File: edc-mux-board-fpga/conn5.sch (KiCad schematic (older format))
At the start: 24 parts

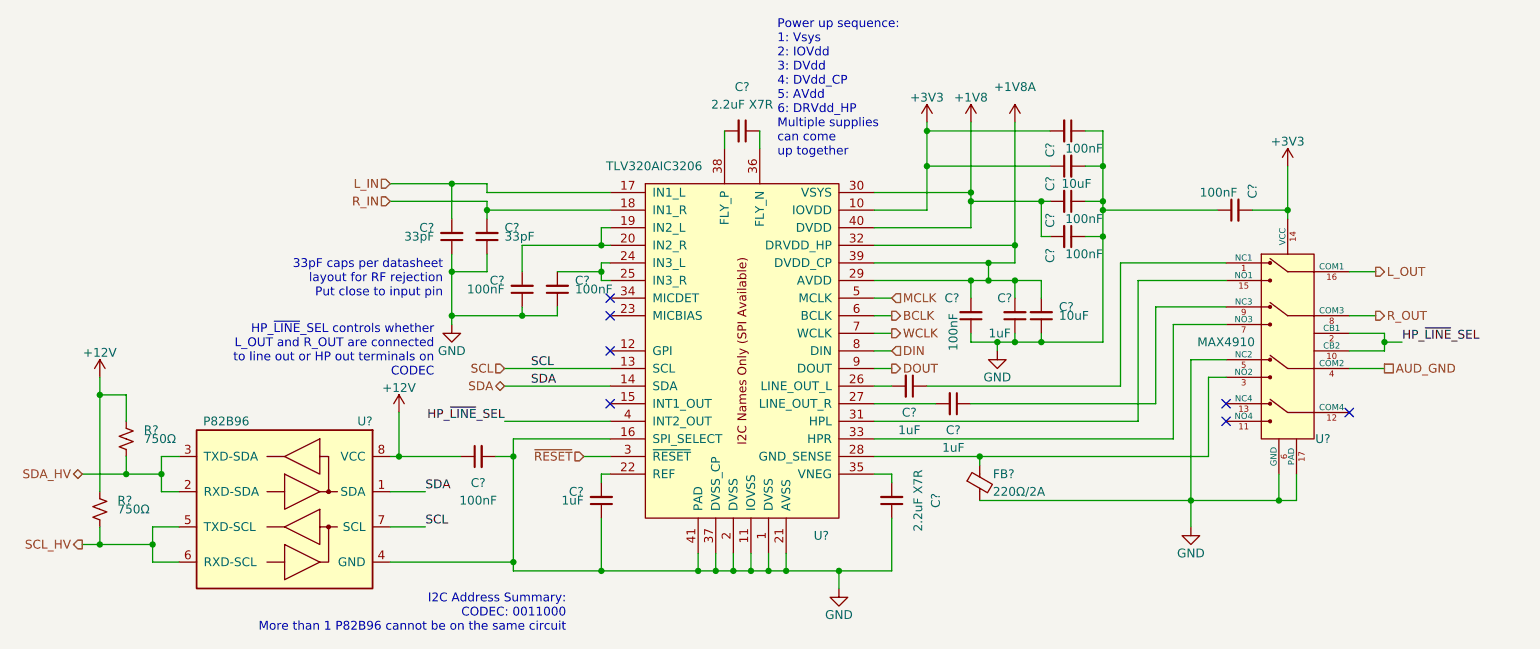
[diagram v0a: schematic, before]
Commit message: Finished FPGA and MCU interconnections.
Finished up interrupt wiring
Fixed a few missing connections
Annotated Schematic
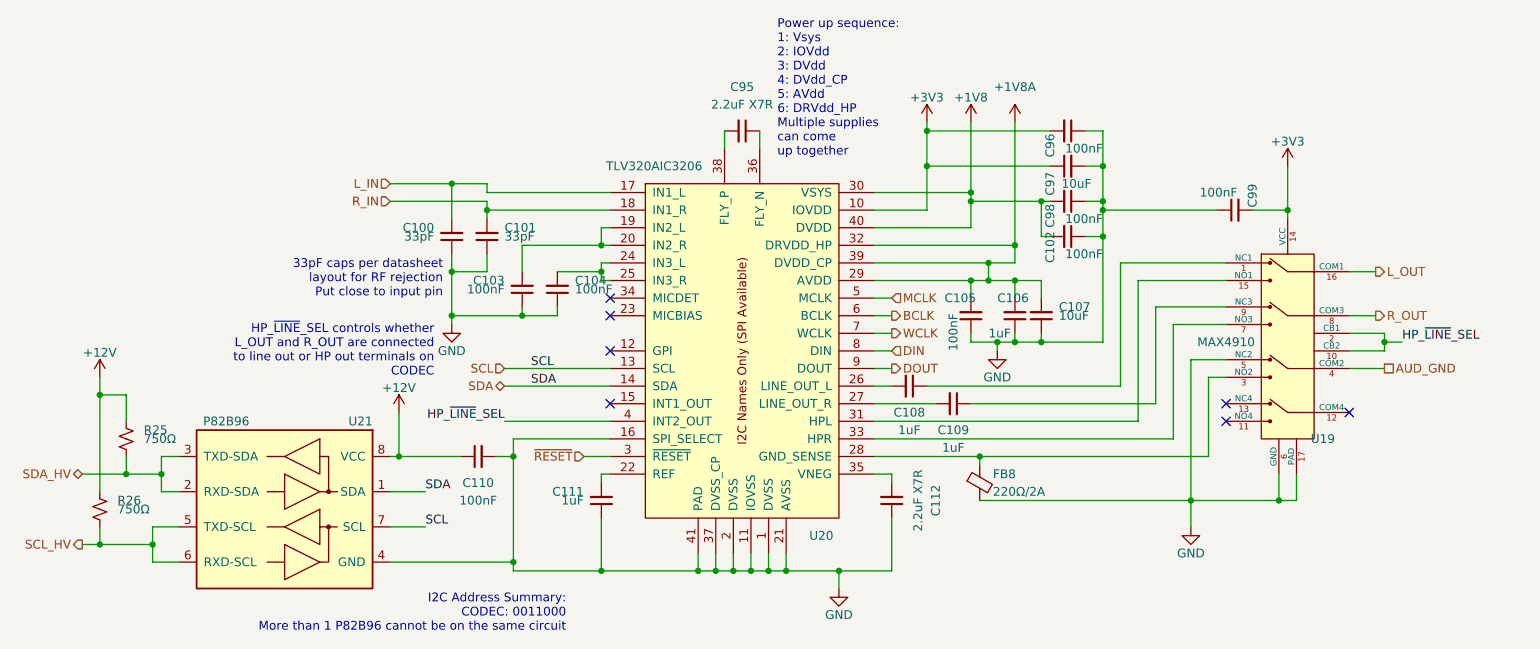
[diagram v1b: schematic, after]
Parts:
- removed C? (x2): 1uF, Capacitor_SMD:C_0805_2012Metric, symbol Device:C_Small
- removed C? (x2): 2.2uF X7R, Capacitor_SMD:C_0603_1608Metric, symbol Device:C_Small
- removed C?: 1uF, Capacitor_SMD:C_0603_1608Metric, symbol Device:C_Small
- removed C? (x8): 100nF, Capacitor_SMD:C_0603_1608Metric, symbol Device:C_Small
- removed C? (x2): 33pF, Capacitor_SMD:C_0603_1608Metric, symbol Device:C_Small
- removed C? (x2): 10uF, Capacitor_SMD:C_1206_3216Metric, symbol Device:C_Small
- removed FB?: 220Ω/2A, Resistor_SMD:R_0603_1608Metric, symbol Device:Ferrite_Bead_Small
- removed R? (x2): 750Ω, Resistor_SMD:R_0603_1608Metric, symbol Device:R_Small_US
- removed U?: TLV320AIC3206, Package_DFN_QFN:UQFN-40-1EP_5x5mm_P0.4mm_EP3.8x3.8mm_ThermalVias, symbol SW-Texas:TLV320AIC3206
- removed U?: MAX4910, Package_DFN_QFN:TQFN-16-1EP_3x3mm_P0.5mm_EP1.23x1.23mm, symbol SW-dallas-semi-maxim:MAX4910
- removed U?: P82B96, Package_SO:TSSOP-8_3x3mm_P0.65mm, symbol Interface_Expansion:P82B96
- added C100, C101: 33pF, Capacitor_SMD:C_0603_1608Metric, symbol Device:C_Small
- added C102, C103, C104, C105, C110, C96, C98, C99: 100nF, Capacitor_SMD:C_0603_1608Metric, symbol Device:C_Small
- added C107, C97: 10uF, Capacitor_SMD:C_1206_3216Metric, symbol Device:C_Small
- added C108, C109: 1uF, Capacitor_SMD:C_0805_2012Metric, symbol Device:C_Small
- added C111: 1uF, Capacitor_SMD:C_0603_1608Metric, symbol Device:C_Small
- added C112, C95: 2.2uF X7R, Capacitor_SMD:C_0603_1608Metric, symbol Device:C_Small
- added FB8: 220Ω/2A, Resistor_SMD:R_0603_1608Metric, symbol Device:Ferrite_Bead_Small
- added R25, R26: 750Ω, Resistor_SMD:R_0603_1608Metric, symbol Device:R_Small_US
- added U19: MAX4910, Package_DFN_QFN:TQFN-16-1EP_3x3mm_P0.5mm_EP1.23x1.23mm, symbol SW-dallas-semi-maxim:MAX4910
- added U20: TLV320AIC3206, Package_DFN_QFN:UQFN-40-1EP_5x5mm_P0.4mm_EP3.8x3.8mm_ThermalVias, symbol SW-Texas:TLV320AIC3206
- added U21: P82B96, Package_SO:TSSOP-8_3x3mm_P0.65mm, symbol Interface_Expansion:P82B96
- gave numbers to parts that had none: 1
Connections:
- net +12V: now also C110.1, R25.1, R26.1, U21.8 (VCC)
- net +1V8: now also C102.2, C98.2, U20.30 (VSYS), U20.40 (DVDD)
- net +1V8A: now also C105.2, C107.2, U20.29 (AVDD), U20.32 (DRVDD_HP), U20.39 (DVDD_CP)
- net +3V3: now also C96.2, C97.1, C99.2, U19.14 (VCC), U20.10 (IOVDD)
- net AUD_GND: now also U19.4 (COM2)
- net BCLK: now also U20.6 (BCLK)
- net DIN: now also U20.8 (DIN)
- net DOUT: now also U20.9 (DOUT)
- net GND: now also C100.1, C101.1, C102.1, C103.1, C104.1, C105.1, C107.1, C110.2, C111.1, C112.1, C96.1, C97.2, C98.1, C99.1, FB8.2, U19.17 (PAD), U19.5 (NC2), U19.6 (GND), U20.1 (DVSS), U20.11 (IOVSS), U20.16 (SPI_SELECT), U20.2 (DVSS), U20.21 (AVSS), U20.37 (DVSS_CP), U20.41 (PAD), U21.4 (GND)
- net HP_~LINE~_SEL: now also U19.10 (CB2), U19.2 (CB1), U20.4 (INT2_OUT)
- net L_IN: now also C100.2, U20.17 (IN1_L)
- net L_OUT: now also U19.16 (COM1)
- net MCLK: now also U20.5 (MCLK)
- net R_IN: now also C101.2, U20.18 (IN1_R)
- net R_OUT: now also U19.8 (COM3)
- net SCL: now also U20.13 (SCL), U21.7 (SCL)
- net SCL_HV: now also R26.2, U21.5 (TXD-SCL), U21.6 (RXD-SCL)
- net SDA: now also U20.14 (SDA), U21.1 (SDA)
- net SDA_HV: now also R25.2, U21.2 (RXD-SDA), U21.3 (TXD-SDA)
- net WCLK: now also U20.7 (WCLK)
- net ~RESET: now also U20.3 (~RESET)
- new net: C108.1, U19.1 (NC1)
- new net: C108.2, U20.26 (LINE_OUT_L)
- new net: C109.1, U19.9 (NC3)
- new net: C109.2, U20.27 (LINE_OUT_R)
- new net: C103.2, U20.19 (IN2_L), U20.20 (IN2_R)
- new net: C111.2, U20.22 (REF)
- new net: C104.2, U20.24 (IN3_L), U20.25 (IN3_R)
- new net: FB8.1, U19.3 (NO2), U20.28 (GND_SENSE)
- new net: U19.15 (NO1), U20.31 (HPL)
- new net: U19.7 (NO3), U20.33 (HPR)
- new net: C112.2, U20.35 (VNEG)
- new net: C95.1, U20.36 (FLY_N)
- new net: C95.2, U20.38 (FLY_P)
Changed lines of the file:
@@
 $EndDescr
 $Comp
-L SW-Texas:TLV320AIC3206 U?
-U 1 1 5CE6F2E7
+L SW-Texas:TLV320AIC3206 U20
+U 1 1 5DAC04B0
 P 5200 3400
-F 0 "U?" H 5650 2350 50  0000 C CNN
+F 0 "U20" H 5650 2350 50  0000 C CNN
 F 1 "TLV320AIC3206" H 4700 4450 50  0000 C CNN
 F 2 "Package_DFN_QFN:UQFN-40-1EP_5x5mm_P0.4mm_EP3.8x3.8mm_ThermalVias" H 5250 4800 50  0001 C CNN
@@
 $EndComp
 $Comp
-L Device:C_Small C?
-U 1 1 5CE6F309
+L Device:C_Small C95
+U 1 1 5DAC04C8
 P 5200 2150
-F 0 "C?" V 4950 2150 50  0000 C CNN
+F 0 "C95" V 4950 2150 50  0000 C CNN
 F 1 "2.2uF X7R" V 5050 2150 50  0000 C CNN
 F 2 "Capacitor_SMD:C_0603_1608Metric" H 5200 2150 50  0001 C CNN
@@
 	5300 2250 5300 2150
 $Comp
-L Device:C_Small C?
-U 1 1 5CE6F311
+L Device:C_Small C112
+U 1 1 5DAC04CE
 P 6050 4250
-F 0 "C?" V 5800 4250 50  0000 C CNN
+F 0 "C112" V 5800 4250 50  0000 C CNN
 F 1 "2.2uF X7R" V 5900 4250 50  0000 C CNN
 F 2 "Capacitor_SMD:C_0603_1608Metric" H 6050 4250 50  0001 C CNN
@@
 	6050 4100 6050 4150
 $Comp
-L power:GND #PWR?
-U 1 1 5CE6F323
+L power:GND #PWR073
+U 1 1 5DAC04E8
 P 5750 4750
-F 0 "#PWR?" H 5750 4500 50  0001 C CNN
+F 0 "#PWR073" H 5750 4500 50  0001 C CNN
 F 1 "GND" H 5750 4600 50  0000 C CNN
 F 2 "" H 5750 4750 50  0001 C CNN
@@
 	5450 4650 5750 4650
 $Comp
-L Device:C_Small C?
-U 1 1 5CE6F329
+L Device:C_Small C111
+U 1 1 5DAC04ED
 P 4400 4250
-F 0 "C?" H 4500 4200 50  0000 L CNN
+F 0 "C111" H 4500 4200 50  0000 L CNN
 F 1 "1uF" H 4500 4250 50  0000 L CNN
 F 2 "Capacitor_SMD:C_0603_1608Metric" H 4400 4250 50  0001 C CNN
@@
 Connection ~ 4950 4650
 $Comp
-L Device:C_Small C?
-U 1 1 5CE6F348
+L Device:C_Small C103
+U 1 1 5DAC04FB
 P 3950 3050
-F 0 "C?" H 4050 3000 50  0000 L CNN
+F 0 "C103" H 4050 3000 50  0000 L CNN
 F 1 "100nF" H 4050 3050 50  0000 L CNN
 F 2 "Capacitor_SMD:C_0603_1608Metric" H 3950 3050 50  0001 C CNN
@@
 $EndComp
 $Comp
-L Device:C_Small C?
-U 1 1 5CE6F363
+L Device:C_Small C104
+U 1 1 5DAC0515
 P 4150 3050
-F 0 "C?" H 4050 3000 50  0000 R CNN
+F 0 "C104" H 4050 3000 50  0000 R CNN
 F 1 "100nF" H 4050 3050 50  0000 R CNN
 F 2 "Capacitor_SMD:C_0603_1608Metric" H 4150 3050 50  0001 C CNN
@@
 Connection ~ 4400 2950
 $Comp
-L power:GND #PWR?
-U 1 1 5CE6F368
+L power:GND #PWR068
+U 1 1 5DAC051A
 P 3550 3250
-F 0 "#PWR?" H 3550 3000 50  0001 C CNN
+F 0 "#PWR068" H 3550 3000 50  0001 C CNN
 F 1 "GND" H 3550 3100 50  0000 C CNN
 F 2 "" H 3550 3250 50  0001 C CNN
@@
 	8650 3300 8850 3300
 $Comp
-L SW-dallas-semi-maxim:MAX4910 U?
-U 1 1 5CE6F375
+L SW-dallas-semi-maxim:MAX4910 U19
+U 1 1 5DAC0532
 P 8300 3350
-F 0 "U?" H 8500 2800 50  0000 C CNN
+F 0 "U19" H 8500 2800 50  0000 C CNN
 F 1 "MAX4910" H 7950 3350 50  0000 C CNN
 F 2 "Package_DFN_QFN:TQFN-16-1EP_3x3mm_P0.5mm_EP1.23x1.23mm" H 9950 4500 50  0001 C CNN
@@
 	7750 3450 7750 4250
 $Comp
-L power:GND #PWR?
-U 1 1 5CE6F387
+L power:GND #PWR072
+U 1 1 5DAC0537
 P 7750 4400
-F 0 "#PWR?" H 7750 4150 50  0001 C CNN
+F 0 "#PWR072" H 7750 4150 50  0001 C CNN
 F 1 "GND" H 7750 4250 50  0000 C CNN
 F 2 "" H 7750 4400 50  0001 C CNN
@@
 	8650 3500 8850 3500
 $Comp
-L Device:Ferrite_Bead_Small FB?
-U 1 1 5CE6F39A
+L Device:Ferrite_Bead_Small FB8
+U 1 1 5DAC054C
 P 6550 4150
-F 0 "FB?" H 6625 4200 50  0000 L CNN
+F 0 "FB8" H 6625 4200 50  0000 L CNN
 F 1 "220Ω/2A" H 6625 4100 50  0000 L CNN
 F 2 "Resistor_SMD:R_0603_1608Metric" V 6480 4150 50  0001 C CNN
@@
 	3750 2600 4450 2600
 $Comp
-L Device:C_Small C?
-U 1 1 5CE6F3AC
+L Device:C_Small C100
+U 1 1 5DAC0553
 P 3550 2750
-F 0 "C?" H 3650 2700 50  0000 L CNN
+F 0 "C100" H 3650 2700 50  0000 L CNN
 F 1 "33pF" H 3650 2750 50  0000 L CNN
 F 2 "Capacitor_SMD:C_0603_1608Metric" H 3550 2750 50  0001 C CNN
@@
 	3200 2550 3750 2550
 $Comp
-L Device:C_Small C?
-U 1 1 5CE6F3B7
+L Device:C_Small C101
+U 1 1 5DAC056F
 P 3750 2750
-F 0 "C?" H 3650 2700 50  0000 R CNN
+F 0 "C101" H 3650 2700 50  0000 R CNN
 F 1 "33pF" H 3650 2750 50  0000 R CNN
 F 2 "Capacitor_SMD:C_0603_1608Metric" H 3750 2750 50  0001 C CNN
@@
 	5950 3000 6500 3000
 $Comp
-L SW-power:+1V8A #+1V8A?
-U 1 1 5CE6F3C8
+L SW-power:+1V8A #+1V8A07
+U 1 1 5DAC0574
 P 6750 2100
-F 0 "#+1V8A?" H 7500 1800 60  0001 C CNN
+F 0 "#+1V8A07" H 7500 1800 60  0001 C CNN
 F 1 "+1V8A" H 6750 2300 50  0000 C CNN
 F 2 "" H 6750 2100 60  0001 C CNN
@@
 $EndComp
 $Comp
-L power:+1V8 #PWR?
-U 1 1 5CE6F3D1
+L power:+1V8 #PWR066
+U 1 1 5DAC0583
 P 6500 2100
-F 0 "#PWR?" H 6500 1950 50  0001 C CNN
+F 0 "#PWR066" H 6500 1950 50  0001 C CNN
 F 1 "+1V8" H 6500 2240 50  0000 C CNN
 F 2 "" H 6500 2100 50  0001 C CNN
@@
 	6750 2800 6750 2900
 $Comp
-L power:+3V3 #PWR?
-U 1 1 5CE6F3E5
+L power:+3V3 #PWR065
+U 1 1 5DAC0598
 P 6250 2100
-F 0 "#PWR?" H 6250 1950 50  0001 C CNN
+F 0 "#PWR065" H 6250 1950 50  0001 C CNN
 F 1 "+3V3" H 6250 2240 50  0000 C CNN
 F 2 "" H 6250 2100 50  0001 C CNN
@@
 	6250 2600 6250 2350
 $Comp
-L Device:C_Small C?
+L Device:C_Small C106
 U 1 1 5CE6F3F4
 P 6750 3200
-F 0 "C?" H 6850 3100 50  0000 R CNN
+F 0 "C106" H 6850 3100 50  0000 R CNN
 F 1 "1uF" H 6900 3300 50  0000 R CNN
 F 2 "Capacitor_SMD:C_0603_1608Metric" H 6750 3200 50  0001 C CNN
@@
 $EndComp
 $Comp
-L power:GND #PWR?
-U 1 1 5CE6F403
+L power:GND #PWR069
+U 1 1 5DAC05AE
 P 6650 3400
-F 0 "#PWR?" H 6650 3150 50  0001 C CNN
+F 0 "#PWR069" H 6650 3150 50  0001 C CNN
 F 1 "GND" H 6650 3250 50  0000 C CNN
 F 2 "" H 6650 3400 50  0001 C CNN
@@
 $EndComp
 $Comp
-L Device:C_Small C?
-U 1 1 5CE6F40F
+L Device:C_Small C107
+U 1 1 5DAC05C8
 P 6900 3200
-F 0 "C?" H 6800 3150 50  0000 R CNN
+F 0 "C107" H 6800 3150 50  0000 R CNN
 F 1 "10uF" H 6800 3200 50  0000 R CNN
 F 2 "Capacitor_SMD:C_1206_3216Metric" H 6900 3200 50  0001 C CNN
@@
 $EndComp
 $Comp
-L Device:C_Small C?
-U 1 1 5CE6F425
+L Device:C_Small C105
+U 1 1 5DAC05CA
 P 6500 3200
-F 0 "C?" H 6650 3100 50  0000 R CNN
+F 0 "C105" H 6650 3100 50  0000 R CNN
 F 1 "100nF" V 6600 3400 50  0000 R CNN
 F 2 "Capacitor_SMD:C_0603_1608Metric" H 6500 3200 50  0001 C CNN
@@
 	6650 3350 6750 3350
 $Comp
-L Device:C_Small C?
-U 1 1 5CE6F42F
+L Device:C_Small C96
+U 1 1 5DAC05DB
 P 7050 2150
-F 0 "C?" H 7200 2050 50  0000 R CNN
+F 0 "C96" H 7200 2050 50  0000 R CNN
 F 1 "100nF" V 7150 2350 50  0000 R CNN
 F 2 "Capacitor_SMD:C_0603_1608Metric" H 7050 2150 50  0001 C CNN
@@
 $EndComp
 $Comp
-L Device:C_Small C?
-U 1 1 5CE6F439
+L Device:C_Small C97
+U 1 1 5DAC05F1
 P 7050 2350
-F 0 "C?" H 6950 2450 50  0000 C CNN
+F 0 "C97" H 6950 2450 50  0000 C CNN
 F 1 "10uF" V 6950 2300 50  0000 C CNN
 F 2 "Capacitor_SMD:C_1206_3216Metric" H 7050 2350 50  0001 C CNN
@@
 	6250 2150 6250 2100
 $Comp
-L Device:C_Small C?
-U 1 1 5CE6F451
+L Device:C_Small C98
+U 1 1 5DAC05FF
 P 7050 2550
-F 0 "C?" H 7200 2450 50  0000 R CNN
+F 0 "C98" H 7200 2450 50  0000 R CNN
 F 1 "100nF" V 7150 2750 50  0000 R CNN
 F 2 "Capacitor_SMD:C_0603_1608Metric" H 7050 2550 50  0001 C CNN
@@
 	6500 2550 6500 2500
 $Comp
-L Device:C_Small C?
-U 1 1 5CE6F456
+L Device:C_Small C102
+U 1 1 5DAC060C
 P 7050 2750
-F 0 "C?" H 7200 2650 50  0000 R CNN
+F 0 "C102" H 7200 2650 50  0000 R CNN
 F 1 "100nF" V 7150 2950 50  0000 R CNN
 F 2 "Capacitor_SMD:C_0603_1608Metric" H 7050 2750 50  0001 C CNN
@@
 NoConn ~ 8650 3750
 $Comp
-L Device:C_Small C?
-U 1 1 5CE6F46F
+L Device:C_Small C99
+U 1 1 5DAC061E
 P 8000 2600
-F 0 "C?" H 8150 2500 50  0000 R CNN
+F 0 "C99" H 8150 2500 50  0000 R CNN
 F 1 "100nF" V 8100 2800 50  0000 R CNN
 F 2 "Capacitor_SMD:C_0603_1608Metric" H 8000 2600 50  0001 C CNN
@@
 $EndComp
 $Comp
-L power:+3V3 #PWR?
-U 1 1 5CE6F47E
+L power:+3V3 #PWR067
+U 1 1 5DAC062E
 P 8300 2350
-F 0 "#PWR?" H 8300 2200 50  0001 C CNN
+F 0 "#PWR067" H 8300 2200 50  0001 C CNN
 F 1 "+3V3" H 8300 2490 50  0000 C CNN
 F 2 "" H 8300 2350 50  0001 C CNN
@@
 	8250 4250 8350 4250
 $Comp
-L Interface_Expansion:P82B96 U?
-U 1 1 5CE6F489
+L Interface_Expansion:P82B96 U21
+U 1 1 5DAC0634
 P 2600 4300
-F 0 "U?" H 2100 4800 50  0000 L CNN
+F 0 "U21" H 2100 4800 50  0000 L CNN
 F 1 "P82B96" H 2800 4800 50  0000 L CNN
 F 2 "Package_SO:TSSOP-8_3x3mm_P0.65mm" H 2600 4300 50  0001 C CNN
@@
 $EndComp
 $Comp
-L power:+12V #PWR?
-U 1 1 5CE6F490
+L power:+12V #PWR070
+U 1 1 5DAC064C
 P 1550 3550
-F 0 "#PWR?" H 1550 3400 50  0001 C CNN
+F 0 "#PWR070" H 1550 3400 50  0001 C CNN
 F 1 "+12V" H 1550 3690 50  0000 C CNN
 F 2 "" H 1550 3550 50  0001 C CNN
@@
 	1900 4100 1900 4200
 $Comp
-L Device:R_Small_US R?
-U 1 1 5CE6F4C1
+L Device:R_Small_US R25
+U 1 1 5DAC065F
 P 1700 3900
-F 0 "R?" H 1800 3950 50  0000 L CNN
+F 0 "R25" H 1800 3950 50  0000 L CNN
 F 1 "750Ω" H 1800 3900 50  0000 L CNN
 F 2 "Resistor_SMD:R_0603_1608Metric" H 1700 3900 50  0001 C CNN
@@
 $EndComp
 $Comp
-L Device:R_Small_US R?
-U 1 1 5CE6F4D0
+L Device:R_Small_US R26
+U 1 1 5DAC0660
 P 1550 4300
-F 0 "R?" H 1650 4350 50  0000 L CNN
+F 0 "R26" H 1650 4350 50  0000 L CNN
 F 1 "750Ω" H 1650 4300 50  0000 L CNN
 F 2 "Resistor_SMD:R_0603_1608Metric" H 1550 4300 50  0001 C CNN
@@
 	1700 4100 1900 4100
 $Comp
-L power:+12V #PWR?
+L power:+12V #PWR071
 U 1 1 5CE6F4E1
 P 3250 3750
-F 0 "#PWR?" H 3250 3600 50  0001 C CNN
+F 0 "#PWR071" H 3250 3600 50  0001 C CNN
 F 1 "+12V" H 3250 3890 50  0000 C CNN
 F 2 "" H 3250 3750 50  0001 C CNN
@@
 	3200 4400 3400 4400
 $Comp
-L Device:C_Small C?
-U 1 1 5CE6F4F3
+L Device:C_Small C110
+U 1 1 5DAC067F
 P 3700 4000
-F 0 "C?" V 3550 4000 50  0000 C CNN
+F 0 "C110" V 3550 4000 50  0000 C CNN
 F 1 "100nF" V 3450 4000 50  0000 C CNN
 F 2 "Capacitor_SMD:C_0603_1608Metric" H 3700 4000 50  0001 C CNN
@@
 	1450 4500 1550 4500
 $Comp
-L Device:C_Small C?
-U 1 1 5CE6F2C0
+L Device:C_Small C108
+U 1 1 5DAC049A
 P 6150 3600
-F 0 "C?" V 6300 3600 50  0000 C CNN
+F 0 "C108" V 6300 3600 50  0000 C CNN
 F 1 "1uF" V 6400 3600 50  0000 C CNN
 F 2 "Capacitor_SMD:C_0805_2012Metric" H 6150 3600 50  0001 C CNN
@@
 $EndComp
 $Comp
-L Device:C_Small C?
-U 1 1 5CE6F2D4
+L Device:C_Small C109
+U 1 1 5DAC04A7
 P 6400 3700
-F 0 "C?" V 6550 3700 50  0000 C CNN
+F 0 "C109" V 6550 3700 50  0000 C CNN
 F 1 "1uF" V 6650 3700 50  0000 C CNN
 F 2 "Capacitor_SMD:C_0805_2012Metric" H 6400 3700 50  0001 C CNN

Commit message: assigned more footprints
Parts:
- C106, C111: value 1uF -> 1uF X7R
- C107, C97: value 10uF -> 10uF X7R
- C108, C109: value 1uF -> 1uF X7R flex
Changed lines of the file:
@@
 P 4400 4250
 F 0 "C111" H 4500 4200 50  0000 L CNN
-F 1 "1uF" H 4500 4250 50  0000 L CNN
+F 1 "1uF X7R" H 4500 4250 50  0000 L CNN
 F 2 "Capacitor_SMD:C_0603_1608Metric" H 4400 4250 50  0001 C CNN
 F 3 "~" H 4400 4250 50  0001 C CNN
@@
 P 6750 3200
 F 0 "C106" H 6850 3100 50  0000 R CNN
-F 1 "1uF" H 6900 3300 50  0000 R CNN
+F 1 "1uF X7R" H 6900 3300 50  0000 R CNN
 F 2 "Capacitor_SMD:C_0603_1608Metric" H 6750 3200 50  0001 C CNN
 F 3 "~" H 6750 3200 50  0001 C CNN
@@
 P 6900 3200
 F 0 "C107" H 6800 3150 50  0000 R CNN
-F 1 "10uF" H 6800 3200 50  0000 R CNN
+F 1 "10uF X7R" H 6800 3200 50  0000 R CNN
 F 2 "Capacitor_SMD:C_1206_3216Metric" H 6900 3200 50  0001 C CNN
 F 3 "~" H 6900 3200 50  0001 C CNN
@@
 P 7050 2350
 F 0 "C97" H 6950 2450 50  0000 C CNN
-F 1 "10uF" V 6950 2300 50  0000 C CNN
+F 1 "10uF X7R" V 6950 2300 50  0000 C CNN
 F 2 "Capacitor_SMD:C_1206_3216Metric" H 7050 2350 50  0001 C CNN
 F 3 "~" H 7050 2350 50  0001 C CNN
@@
 P 6150 3600
 F 0 "C108" V 6300 3600 50  0000 C CNN
-F 1 "1uF" V 6400 3600 50  0000 C CNN
+F 1 "1uF X7R flex" V 6400 3600 50  0000 C CNN
 F 2 "Capacitor_SMD:C_0805_2012Metric" H 6150 3600 50  0001 C CNN
 F 3 "~" H 6150 3600 50  0001 C CNN
@@
 P 6400 3700
 F 0 "C109" V 6550 3700 50  0000 C CNN
-F 1 "1uF" V 6650 3700 50  0000 C CNN
+F 1 "1uF X7R flex" V 6650 3700 50  0000 C CNN
 F 2 "Capacitor_SMD:C_0805_2012Metric" H 6400 3700 50  0001 C CNN
 F 3 "~" H 6400 3700 50  0001 C CNN
